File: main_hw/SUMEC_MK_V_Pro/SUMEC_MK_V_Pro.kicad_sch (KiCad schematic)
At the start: 134 parts, among them J1 XT30PW-M, J10 Conn_01x03_Pin, J11 Conn_01x03_Pin, J12 Conn_01x06_Pin, J13 Conn_01x03_Pin, J2 Conn_01x06_Socket, J3 Conn_01x06_Socket, J4 USB_C, J5 Conn_01x03_Pin, J6 Conn_01x04_Pin, J7 Conn_01x03_Pin, J8 Conn_01x03_Pin, J9 Conn_01x03_Pin, Q1 PMOS, SW1 SW_DPDT_x2, SW2 RST, SW3 RESET, SW4 BOOT, SW5 BOOT, SW6 BOOT, U1 INA226, U2 DRV8874PWPR, U3 DRV8874PWPR, U4 AP62300Z6, U5 TPS565242DRLR, U6 USBLC6-2SC6, U7 BNO055, U8 ESP32-S3-WROOM-1, U9 24CW1280T-I/OT, Y1 32.768k

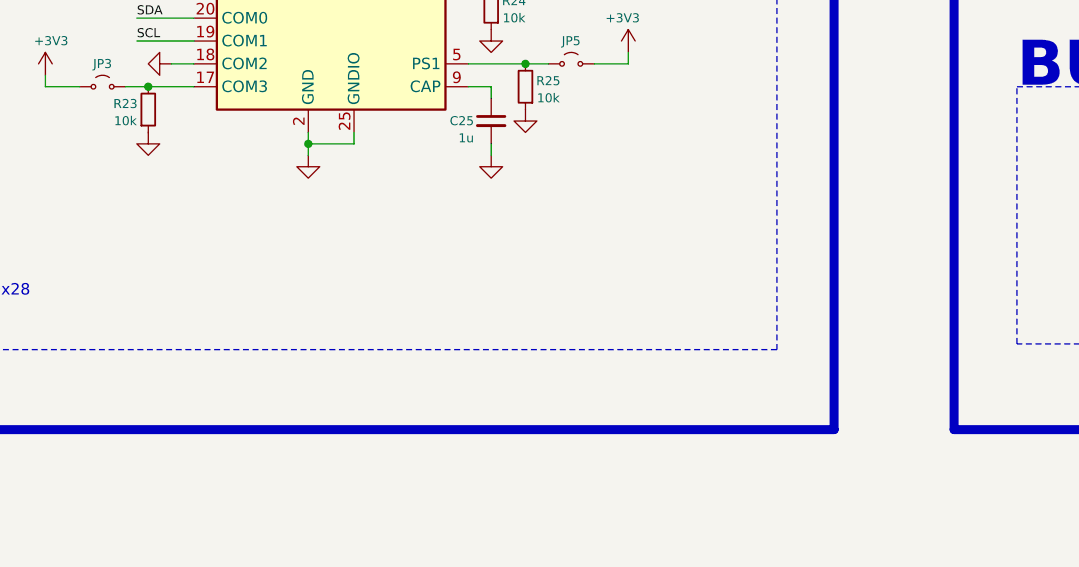
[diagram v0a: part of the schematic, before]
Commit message: Update SUMEC_MK_V_Pro.kicad_sch
Added description for PS1 and PS0 pins of BN055 IMU onboard sensor.
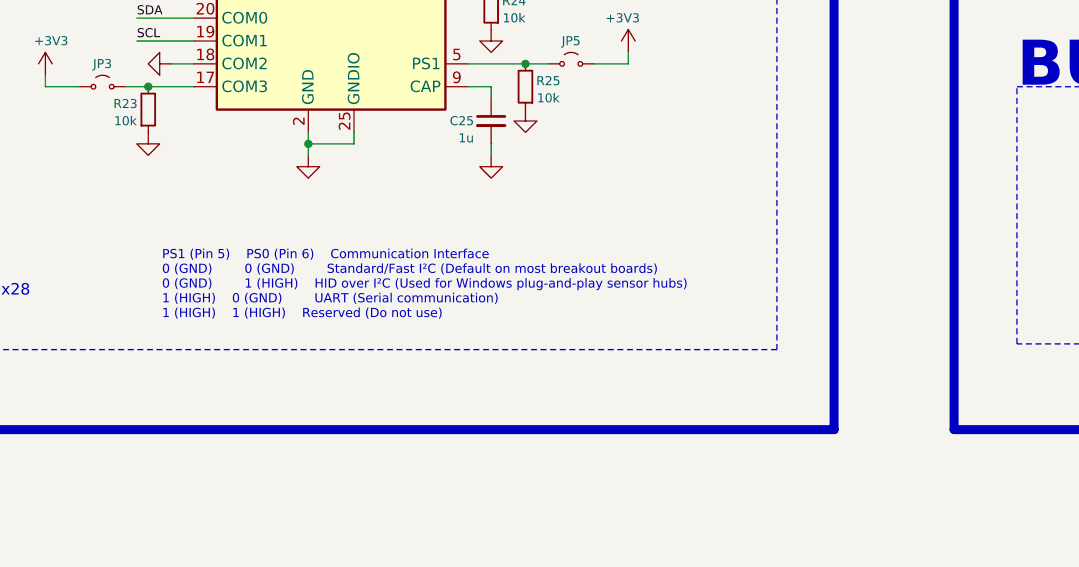
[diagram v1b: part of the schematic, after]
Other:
- note added: "PS1 (Pin 5) PS0 (Pin 6) Communication Interface 0 (GND) 0 (GND) Standard/Fast I²C (Default on most breakout boards) 0 (GND) 1 (HIGH) HID over I²C (Used for Windows plug-and-play sensor hubs) 1 (HIGH) 0 (GND) UART (Serial communication) 1 (HIGH) 1 (HIGH) Reserved (Do not use)"
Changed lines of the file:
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@@
+		)
+	)
+	(text "PS1 (Pin 5)	PS0 (Pin 6)	Communication Interface\n0 (GND)		0 (GND)		Standard/Fast I²C (Default on most breakout boards)\n0 (GND)		1 (HIGH)	HID over I²C (Used for Windows plug-and-play sensor hubs)\n1 (HIGH)	0 (GND)		UART (Serial communication)\n1 (HIGH)	1 (HIGH)	Reserved (Do not use)"
+		(exclude_from_sim no)
+		(at 288.544 335.788 0)
+		(effects
+			(font
+				(face "Courier New")
+				(size 1.016 1.016)
+				(color 0 72 0 1)
+			)
+			(justify left)
 		)
 	)

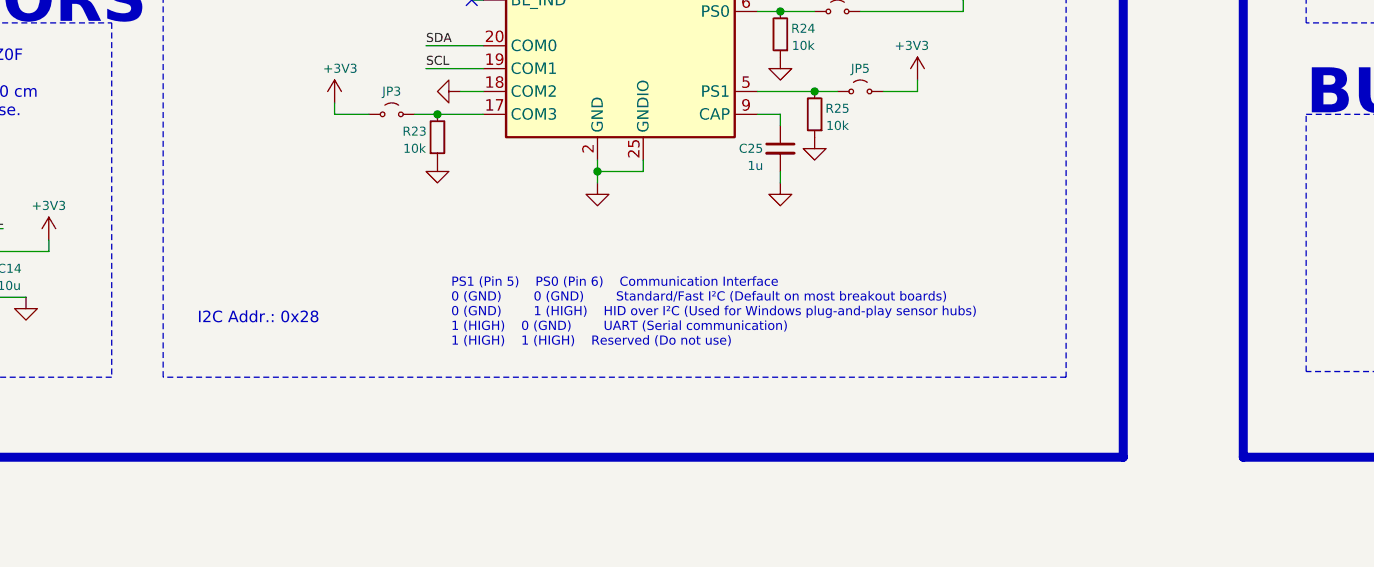
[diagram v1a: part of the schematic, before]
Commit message: Update SUMEC_MK_V_Pro.kicad_sch
Added description for COM3 pin of BN055 for I2C address selection.
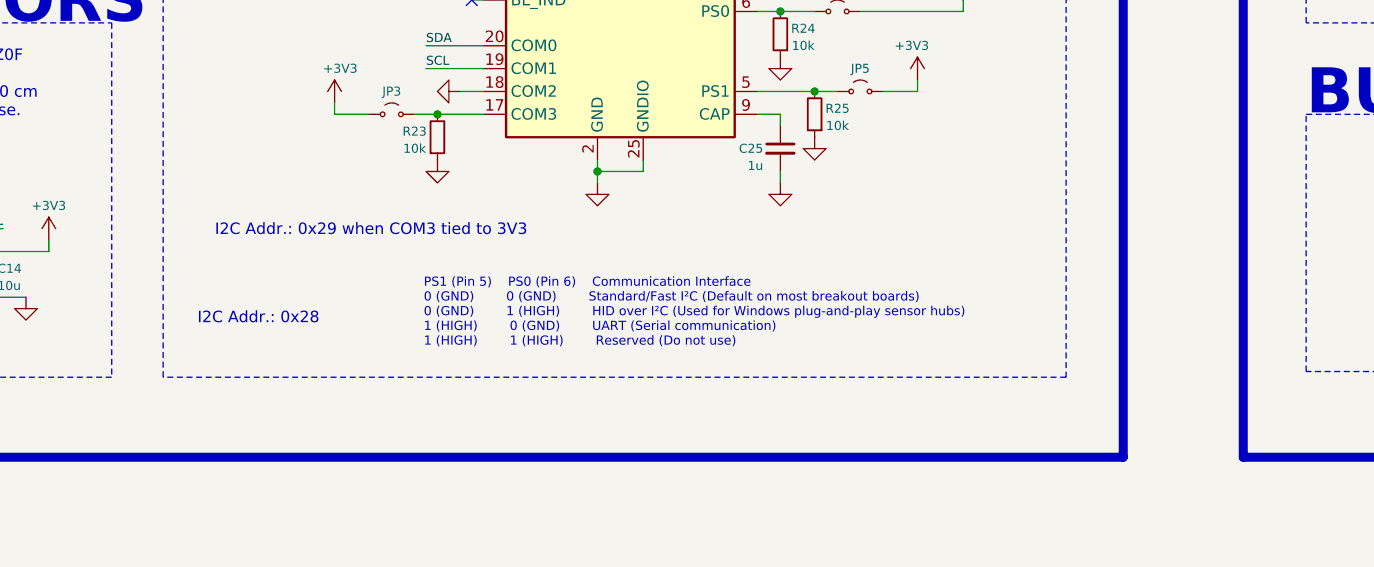
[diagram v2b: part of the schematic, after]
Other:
- note added: "I2C Addr.: 0x29 when COM3 tied to 3V3"
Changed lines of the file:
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@@
 		)
 	)
-	(text "PS1 (Pin 5)	PS0 (Pin 6)	Communication Interface\n0 (GND)		0 (GND)		Standard/Fast I²C (Default on most breakout boards)\n0 (GND)		1 (HIGH)	HID over I²C (Used for Windows plug-and-play sensor hubs)\n1 (HIGH)	0 (GND)		UART (Serial communication)\n1 (HIGH)	1 (HIGH)	Reserved (Do not use)"
+	(text "PS1 (Pin 5)	PS0 (Pin 6)	Communication Interface\n0 (GND)		0 (GND)		Standard/Fast I²C (Default on most breakout boards)\n0 (GND)		1 (HIGH)		HID over I²C (Used for Windows plug-and-play sensor hubs)\n1 (HIGH)		0 (GND)		UART (Serial communication)\n1 (HIGH)		1 (HIGH)		Reserved (Do not use)"
 		(exclude_from_sim no)
-		(at 288.544 335.788 0)
+		(at 285.496 335.788 0)
 		(effects
 			(font
@@
 		)
 	)
+	(text "I2C Addr.: 0x29 when COM3 tied to 3V3"
+		(exclude_from_sim no)
+		(at 279.654 326.644 0)
+		(effects
+			(font
+				(size 1.27 1.27)
+			)
+		)
+	)
